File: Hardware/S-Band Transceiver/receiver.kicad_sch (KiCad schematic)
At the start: 63 parts, among them J6 SMA, J7 SMA, J8 SMA, U13 LT1819, U14 LT1819, U15 ADL5380, U16 TSS-53LNB3+, U17 SN74LVC1G125DCK, U18 SKY16603-632LF, U19 DCW-22-332+, U20 ADL5906

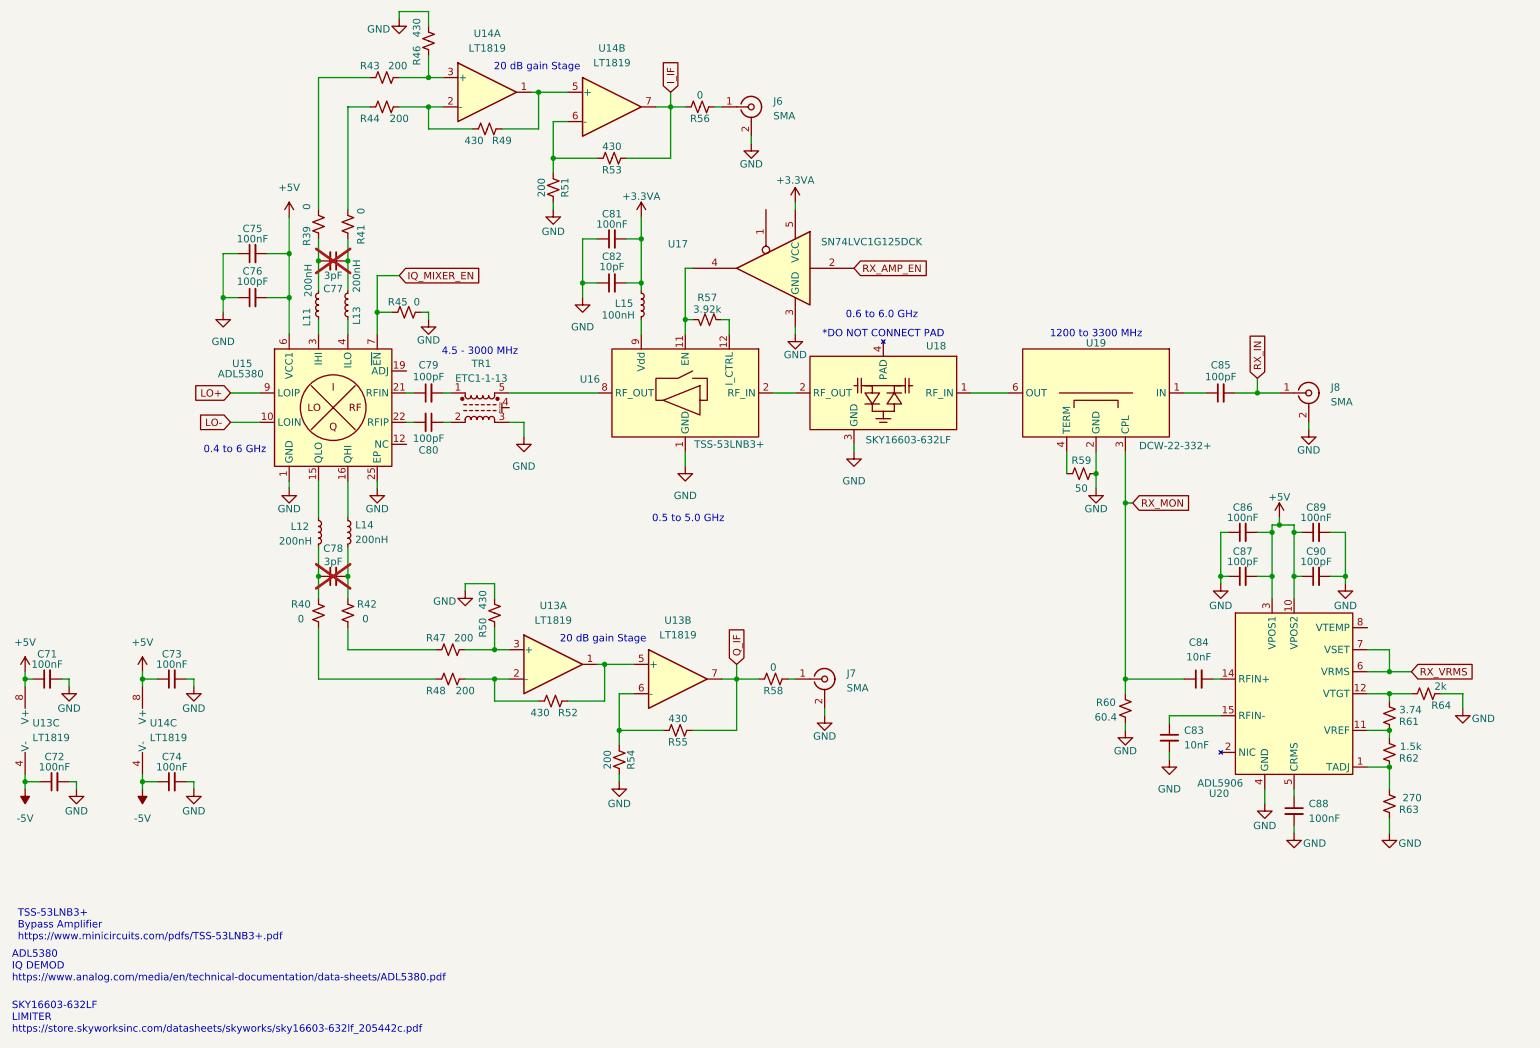
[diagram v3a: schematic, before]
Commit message: Updating Capacitors and LEDs in schematic
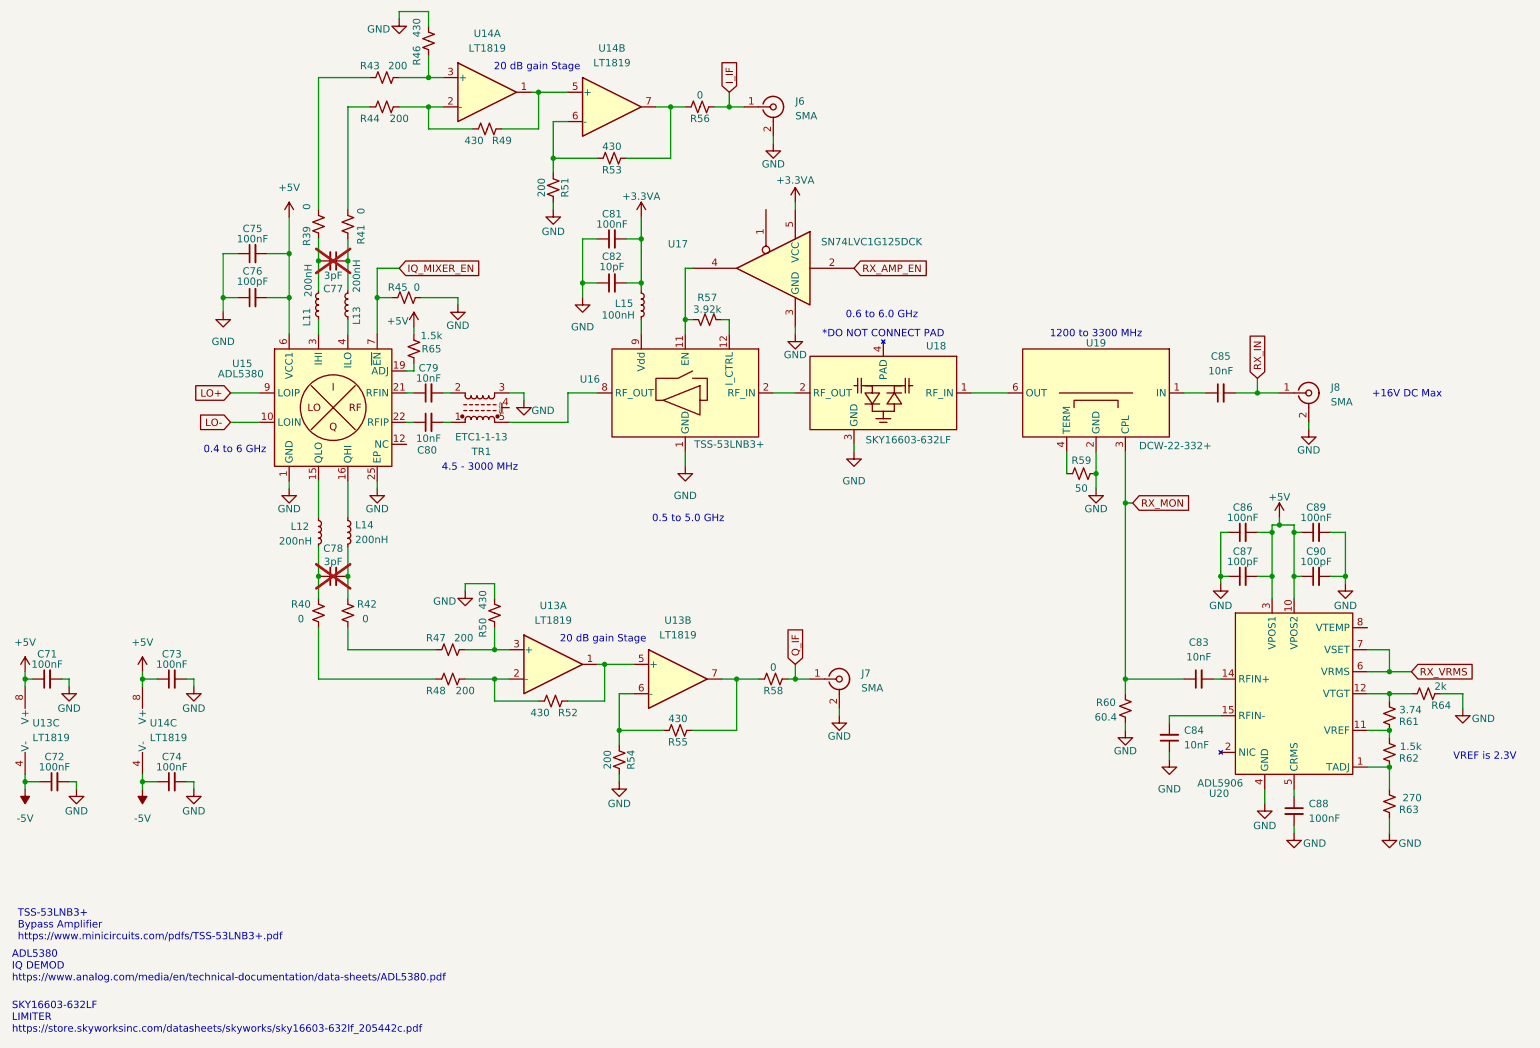
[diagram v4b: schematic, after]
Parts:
- added R65: 1.5k, Resistor_SMD:R_0603_1608Metric, symbol Device:R_Small_US
- C79, C80, C85: value 100pF -> 10nF; Digikey (none) -> 1284-1540-1-ND
- C83, C84: Digikey (none) -> 1284-1540-1-ND
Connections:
- net +5V: now also R65.1
- net GND: now also C84.1; no longer C83.2
- net I_IF: now also J6.1 (In), R56.2; no longer R53.2, R56.1, U14.7
- net Q_IF: now also J7.1 (In), R58.2; no longer R55.2, R58.1, U13.7
- net RX_MON: now also C83.1; no longer C84.1
- net at TR1.1: now also C80.2; no longer C79.2
- net at TR1.2: now also C79.2; no longer C80.1
- net at U20.14 (RFIN+): now also C83.2; no longer C84.2
- net at U15.19 (ADJ): now also R65.2
- net at U15.22 (RFIP): now also C80.1; no longer C80.2
- net at U20.15 (RFIN-): now also C84.2; no longer C83.1
- new net: R55.2, R58.1, U13.7
- new net: R53.2, R56.1, U14.7
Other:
- note added: "+16V DC Max"
- note added: "VREF is 2.3V"
- moved on the sheet: J6, J7, R45

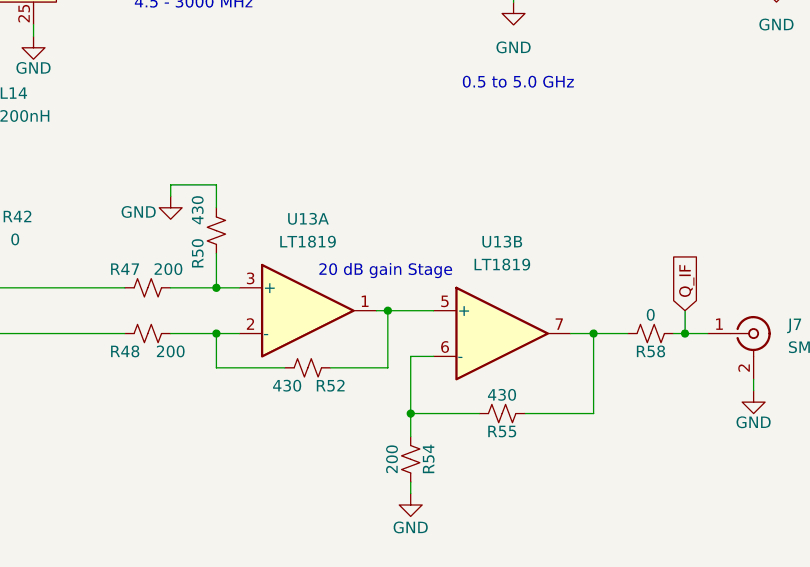
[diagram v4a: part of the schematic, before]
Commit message: Updating synthesizer schematic and layout
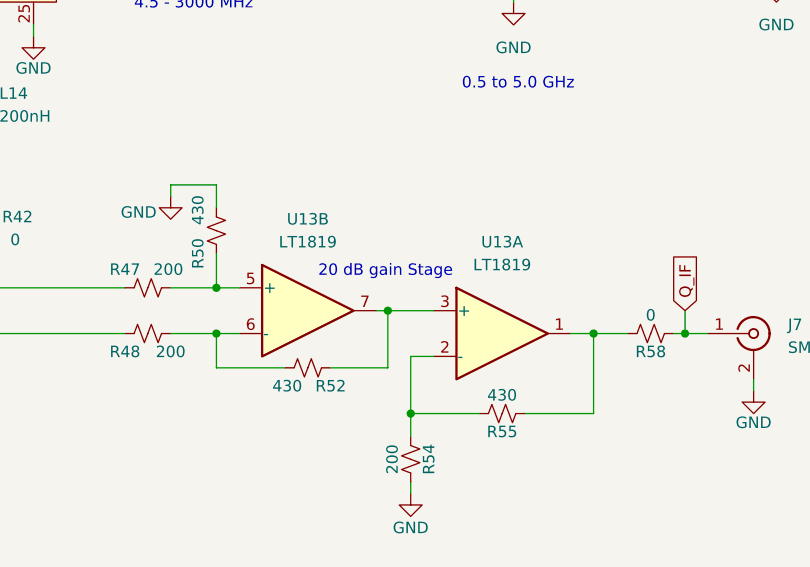
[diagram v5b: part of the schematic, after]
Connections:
- net at R55.2, R58.1: now also U13.1; no longer U13.7
- net at R54.2, R55.1: now also U13.2 (-); no longer U13.6 (-)
- net at R47.1, R50.2: now also U13.5 (+); no longer U13.3 (+)
- net at R48.1, R52.1: now also U13.6 (-); no longer U13.2 (-)
- new net: R52.2, U13.3 (+), U13.7
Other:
- moved on the sheet: U13A, U13B

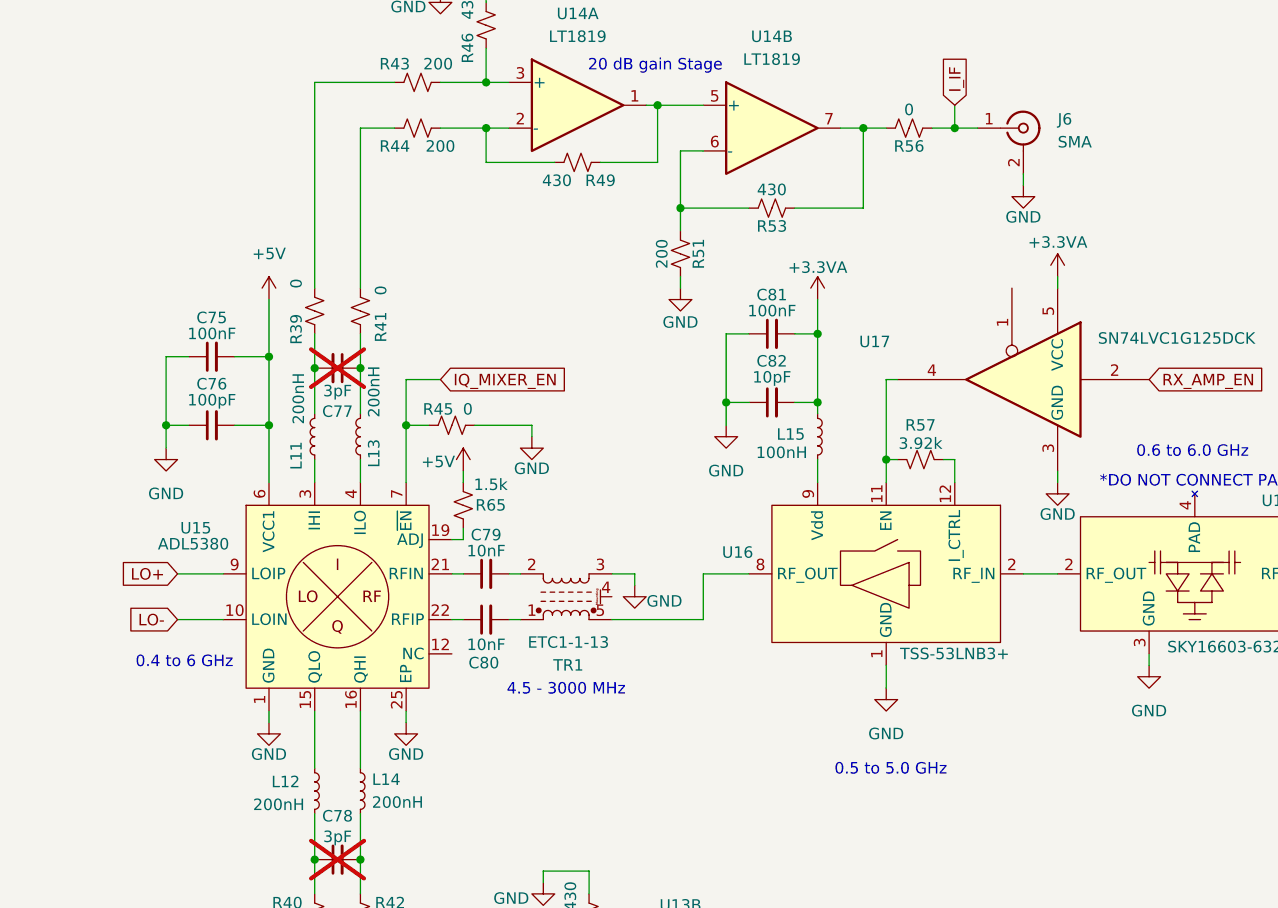
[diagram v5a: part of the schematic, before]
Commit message: Updating board layout, adding inductor to LNA input
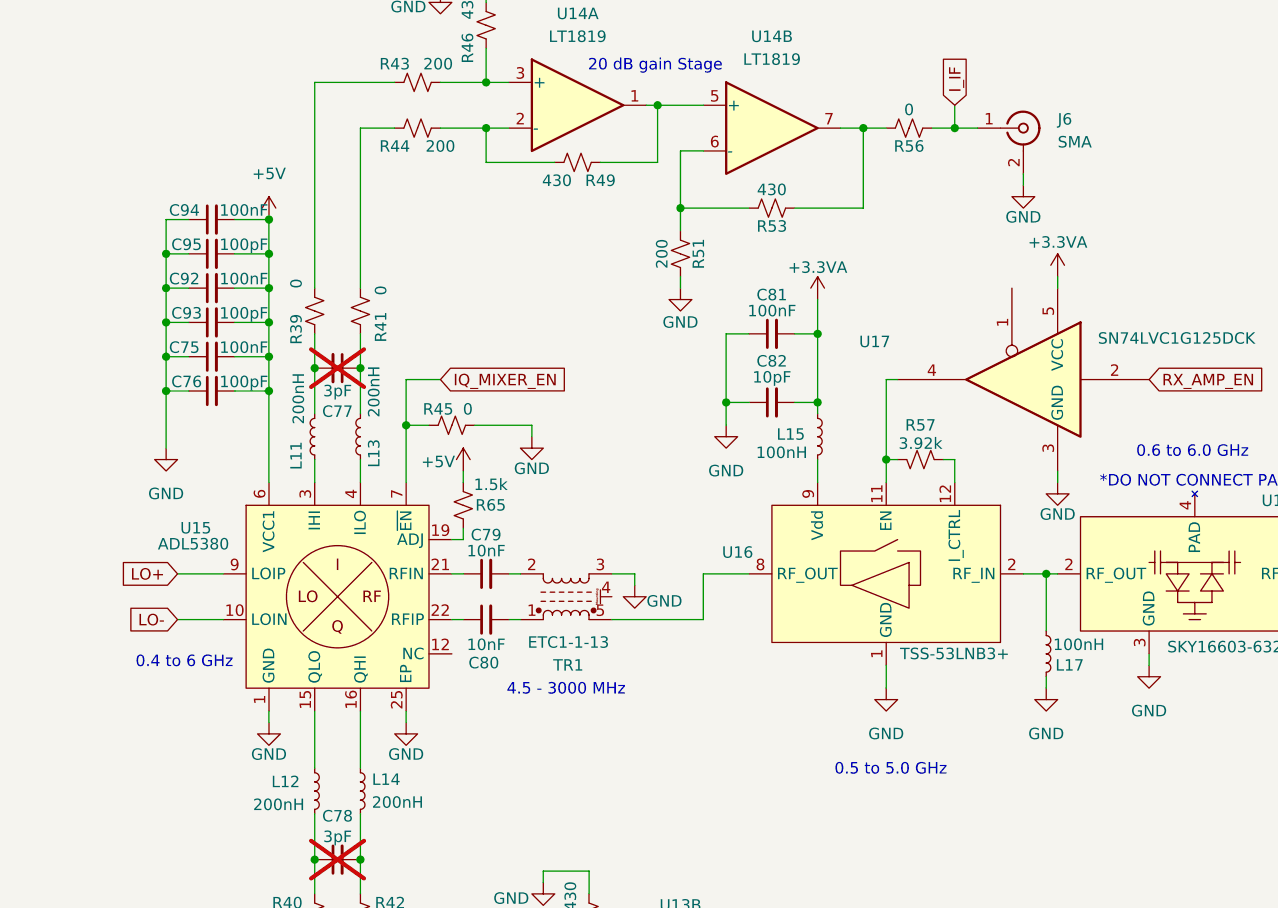
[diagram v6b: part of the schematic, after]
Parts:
- added C92, C94: 100nF, Capacitor_SMD:C_0402_1005Metric, symbol Device:C_Small
- added C93, C95: 100pF, Capacitor_SMD:C_0402_1005Metric, symbol Device:C_Small
- added L17: 100nH, Inductor_SMD:L_0402_1005Metric, symbol Device:L_Small
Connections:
- net +5V: now also C92.2, C93.2, C94.2, C95.2
- net GND: now also C92.1, C93.1, C94.1, C95.1, L17.2
- net at U16.2 (RF_IN), U18.2 (RF_OUT): now also L17.1
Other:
- moved on the sheet: C76

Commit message: Starting to route board
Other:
- note added: "ADL5380 Evaluation board uses baluns for I and Q outputs"
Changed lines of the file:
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@@
+		)
+	)
+	(text "ADL5380 Evaluation board\nuses baluns for I and Q outputs"
+		(exclude_from_sim no)
+		(at 37.846 101.6 0)
+		(effects
+			(font
+				(size 1.27 1.27)
+			)
 		)
 	)

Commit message: Updating board layout and routing
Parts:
- R45: value 0 -> 10k; now not fitted
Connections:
- net I_IF: now also J7.1 (In); no longer J6.1 (In)
- net Q_IF: now also J6.1 (In); no longer J7.1 (In)
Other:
- moved on the sheet: J6, J7
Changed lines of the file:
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@@
 	(symbol
 		(lib_id "Connector:Conn_Coaxial")
-		(at 161.29 132.08 0)
+		(at 149.86 33.02 0)
 		(unit 1)
 		(exclude_from_sim no)
@@
 		(fields_autoplaced yes)
 		(property "Reference" "J7"
-			(at 165.1 131.1031 0)
+			(at 153.67 32.0431 0)
 			(effects
 				(font
@@
 		)
 		(property "Value" "SMA"
-			(at 165.1 133.6431 0)
+			(at 153.67 34.5831 0)
 			(effects
 				(font
@@
 		)
 		(property "Footprint" "Connector_Coaxial:SMA_Samtec_SMA-J-P-X-ST-EM1_EdgeMount"
-			(at 161.29 132.08 0)
+			(at 149.86 33.02 0)
 			(effects
 				(font
@@
 		)
 		(property "Datasheet" " ~"
-			(at 161.29 132.08 0)
+			(at 149.86 33.02 0)
 			(effects
 				(font
@@
 		)
 		(property "Description" "coaxial connector (BNC, SMA, SMB, SMC, Cinch/RCA, LEMO, ...)"
-			(at 161.29 132.08 0)
+			(at 149.86 33.02 0)
 			(effects
 				(font
@@
 	(symbol
 		(lib_id "Connector:Conn_Coaxial")
-		(at 149.86 33.02 0)
+		(at 161.29 132.08 0)
 		(unit 1)
 		(exclude_from_sim no)
@@
 		(fields_autoplaced yes)
 		(property "Reference" "J6"
-			(at 153.67 32.0431 0)
+			(at 165.1 131.1031 0)
 			(effects
 				(font
@@
 		)
 		(property "Value" "SMA"
-			(at 153.67 34.5831 0)
+			(at 165.1 133.6431 0)
 			(effects
 				(font
@@
 		)
 		(property "Footprint" "Connector_Coaxial:SMA_Samtec_SMA-J-P-X-ST-EM1_EdgeMount"
-			(at 149.86 33.02 0)
+			(at 161.29 132.08 0)
 			(effects
 				(font
@@
 		)
 		(property "Datasheet" " ~"
-			(at 149.86 33.02 0)
+			(at 161.29 132.08 0)
 			(effects
 				(font
@@
 		)
 		(property "Description" "coaxial connector (BNC, SMA, SMB, SMC, Cinch/RCA, LEMO, ...)"
-			(at 149.86 33.02 0)
+			(at 161.29 132.08 0)
 			(effects
 				(font
@@
 		(in_bom yes)
 		(on_board yes)
-		(dnp no)
+		(dnp yes)
 		(property "Reference" "R45"
 			(at 84.836 64.262 90)
@@
 			)
 		)
-		(property "Value" "0"
-			(at 88.138 64.262 90)
-			(effects
-				(font
+		(property "Value" "10k"
+			(at 88.646 64.262 90)
+			(effects
+				(font
